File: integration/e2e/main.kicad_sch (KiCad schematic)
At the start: 1 part, among them J1 Power

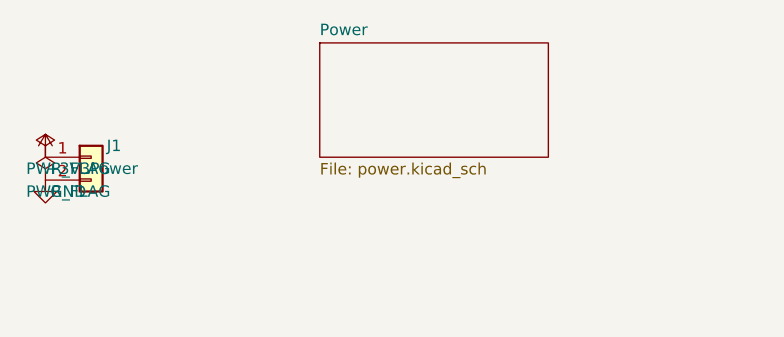
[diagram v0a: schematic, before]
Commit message: feat(e2e): lay out the e2e schematic with straight wires
The first e2e sheets connected parts pin to pin, on A4: correct (ERC
clean) but hard to read, with parts on top of each other in a corner.
Now:

* both sheets are A5, with title blocks (title, date, revision, a note);
* every wire is straight. On the root sheet, each pin of J1 runs left
  to its rail, +3V3 and its power flag above, GND and its flag below,
  with a junction on each rail. On "Power", +3V3, R1, D1 (turned so its
  anode is on top) and GND form one column;
* D1's reference and value read horizontally.

The nets, parts and UUIDs are unchanged, so the board still matches.
KiCad 9.0.9, on the design staged as kicad_pcb stages it: ERC 0
violations; DRC 0 violations, 0 unconnected, 0 parity issues; netlist
+3V3 (J1.1, R1.1), GND (D1.K, J1.2), Net-(D1-A) (D1.A, R1.2).

This commit has been created by an automated coding assistant,
with human supervision.

Prompt:
why do these sample e2e designs have doglegs in schematics, when all
wires could be mostly straight?

Co-Authored-By: Claude Opus 5.5 <noreply@anthropic.com>
Claude-Session: https://claude.ai/code/session_01WoWXzhMvNxH4iJRPTWT44f
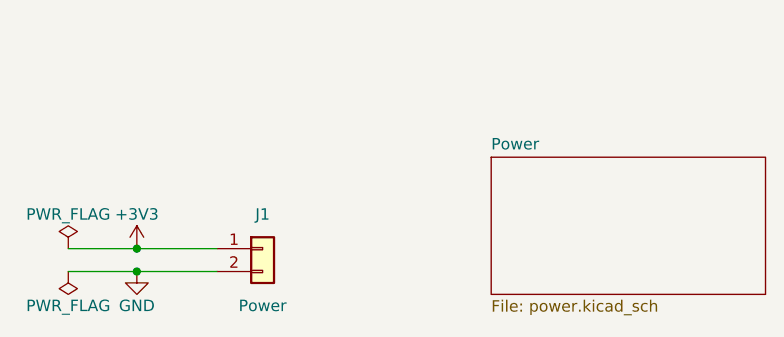
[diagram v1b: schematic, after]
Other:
- company: (none) -> rules_kicad
- title: (none) -> rules_kicad e2e design
- moved on the sheet: J1
